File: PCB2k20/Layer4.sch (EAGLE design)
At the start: 32 parts

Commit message: Layer 4: linked with fusion so its easier to move stuff around
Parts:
- removed 1R2: 1k, JH:RESISTOR0603
- removed 1R3: 10k, JH:RESISTOR0603
- removed 1S1: 34-MOMENTARY-SWITCH, JH:34-MOMENTARY-SWITCH
- added J1, J2: CONN_03, JH:CONN_03
- added J3: (no value), SparkFun-Connectors:CONN_05LOCK
- added R1: 10k, JH:RESISTOR0603
- added U$1: 74HCT08, JH:74HCT08
- 1S2: value 34-MOMENTARY-SWITCH -> MOMENTARY_SWITCH_4X3; device JH:34-MOMENTARY-SWITCH -> JH:MOMENTARY_SWITCH_4X3
- D1, D10, D11, D12, D13, D14, D15, D16, D2, D3, D4, D5, D6, D7, D8, D9: device SparkFun-LED:WS2812B -> JH:WS2812B
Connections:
- net 15 renamed SDA
- net 16 renamed SCL
- net 17 renamed TOF3_XSHUT
- net 18 renamed TOF3_GPIO
- net 19 renamed TOF4_XSHUT
- net 20 renamed TOF4_GPIO
- net 28 renamed TOF1_XSHUT
- net 29 renamed TOF1_GPIO
- net 30 renamed TOF2_XSHUT
- net 31 renamed TOF2_GPIO
- removed net 0: 1U1.PB11/I2C2_SDA/USART3_RX
- removed net 1: 1U1.PB10/I2C2_SCL/USART3_TX
- removed net 10: 1U1.PA1/USART2_RTS/ADC12_IN1/TIM2_CH2
- removed net 11: 1U1.PA0_WKUP/USART2_CTS/ADC12_IN0/TIM2_CH1_ETR
- removed net 12: 1U1.PC15-OSC32_OUT
- removed net 13: 1U1.PC14-OSC32_IN
- removed net 14: 1U1.PC13-TAMPER-RTC
- removed net 2: 1U1.PB2/BOOT1
- removed net 23_USBDP: 1U1.PA12/USART1_RTS/CAN_TX/TIM1_ETR/USBDP
- removed net 24_USBDM: 1U1.PA11/USART1_CTS/CAN_RX/TIM1_CH4/USBDM
- removed net 25: 1U1.PA10/USART1_RX/TIM1_CH3
- removed net 26: 1U1.PA9/USART1_TX/TIM1_CH2
- removed net 27: 1U1.PA8/USART1_CK/TIM1_CH1/MCO
- removed net 3: 1U1.PB0/ADC12_IN8/TIM3_CH3
- removed net 32: 1R3.2, 1S1.2, 1U1.BOOT0, 1U1.PB8/TIM4_CH3
- removed net 4: 1U1.PA7/SPI1_MOSI/ADC12_IN7/TIM3_CH2
- removed net 5: 1U1.PA6/SPI1_MISO/ADC12_IN6/TIM3_CH1
- removed net 6: 1U1.PA5/SPI1_SCK/ADC12_IN5
- removed net 7: 1U1.PA4/SPI1_NSS/USART2_CK/ADC12_IN4
- removed net 8: 1U1.PA3/USART2_RX/ADC12_IN3/TIM2_CH4
- removed net 9: 1U1.PA2/USART2_TX/ADC12_IN2/TIM2_CH3
- removed net DISC: 1U1.PB9/TIM4_CH4
- removed net N$1: 1R2.1, 1S1.1
- removed net VBAT: 1U1.VBAT
- new net 5V: J3.5, U$1G1.I1, U$1G2.I1, U$1G3.I1, U$1G5.P$V+
- new net ESC1_IN: 1U1.PA8/USART1_CK/TIM1_CH1/MCO, U$1G2.I0
- new net ESC1_OUT: J1.3, U$1G2.O
- new net ESC2_IN: 1U1.PA1/USART2_RTS/ADC12_IN1/TIM2_CH2, U$1G3.I0
- new net ESC2_OUT: J2.3, U$1G3.O
- new net N$23: 1U1.BOOT0, R1.1
- new net USART1_RX: 1U1.PA10/USART1_RX/TIM1_CH3, J3.3
- new net USART1_TX: 1U1.PA9/USART1_TX/TIM1_CH2, J3.2
- new net WS2812B: 1U1.PA7/SPI1_MOSI/ADC12_IN7/TIM3_CH2, U$1G1.I0
- new net WS2812B_OUT: D1.DI, U$1G1.O
- net 3.3V: now also J3.4; no longer 1R2.2
- net GND: now also J1.1, J2.1, J3.1, R1.2, U$1G5.P$V-; no longer 1R3.1
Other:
- note removed: "BOOT0"
- moved on the sheet: 1D1, 1R1, SWD

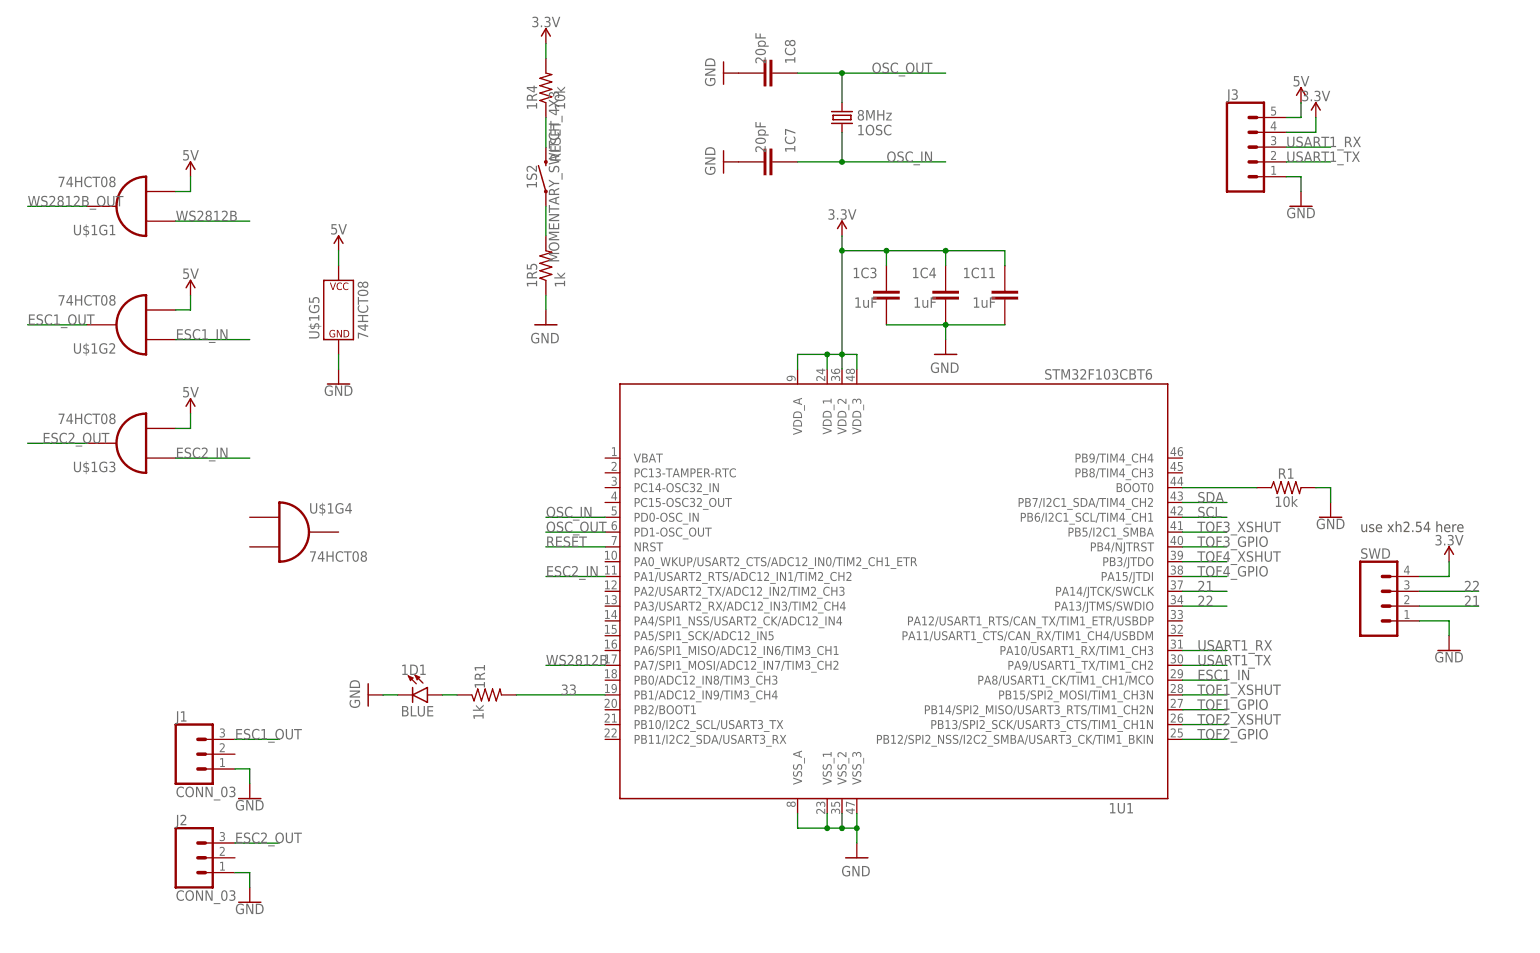
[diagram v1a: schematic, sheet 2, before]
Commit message: finish layer 4 and start on layer 3, TODO: silkscreen for layer4
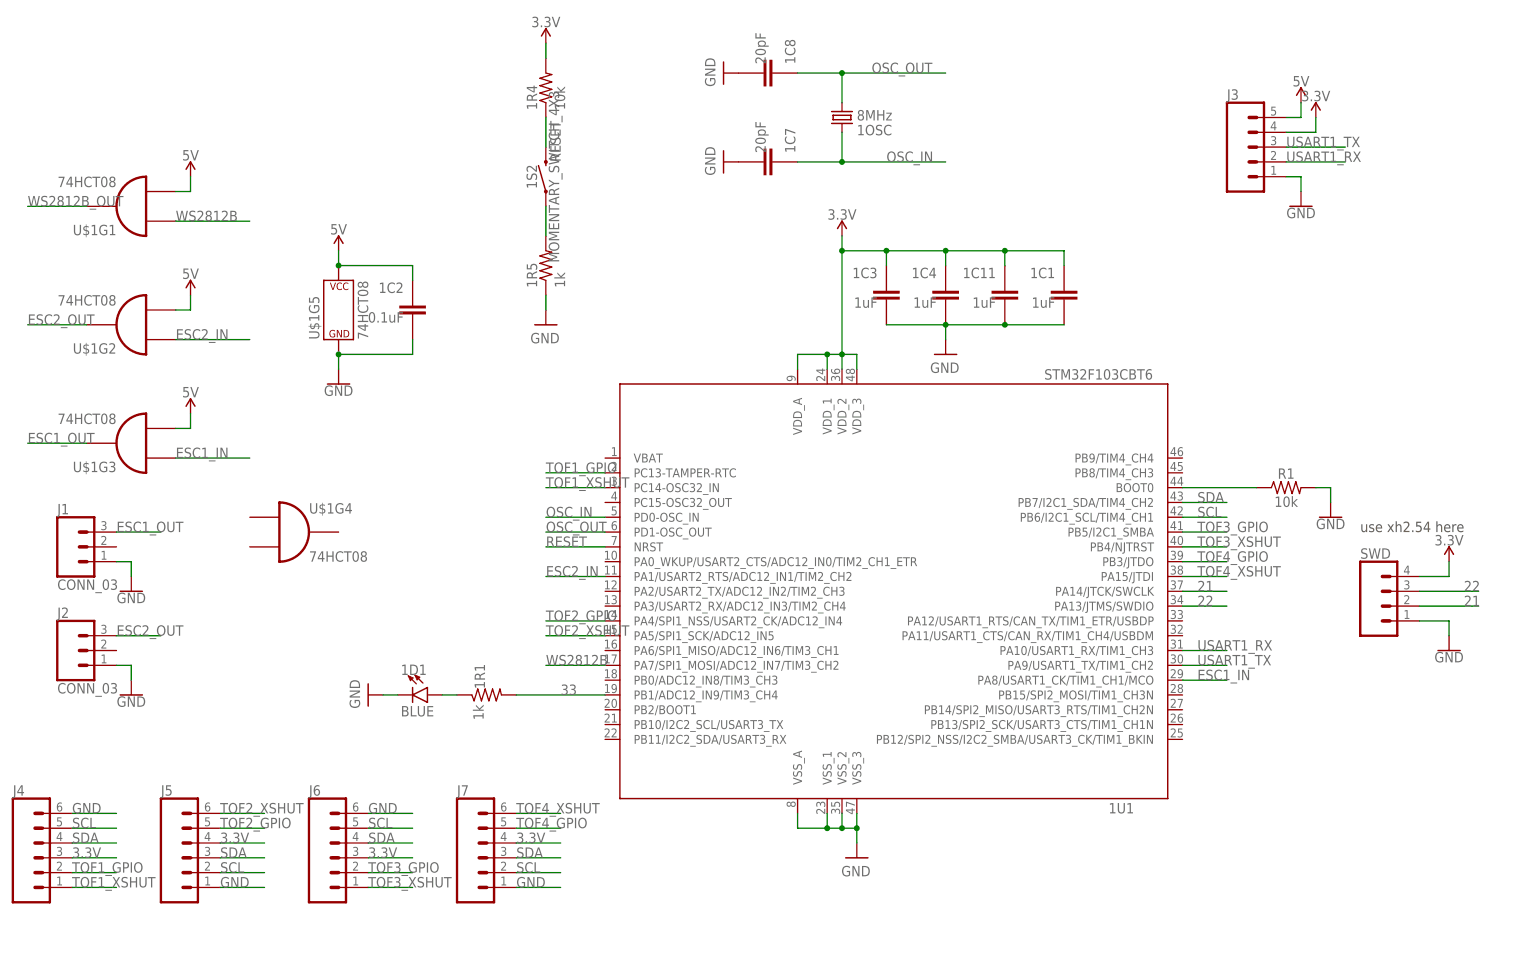
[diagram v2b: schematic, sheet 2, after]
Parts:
- added 1C1: 1uF, JH:CAPACITOR0603
- added 1C2, AC1, AC2, AC3, AC4, AC5, AC6, AC7, AC8, C1, C11, C13, C15, C3, C5, C7, C9: 0.1uF, JH:CAPACITOR0603
- added J4, J5, J6, J7: (no value), SparkFun-Connectors:CONN_06LOCK
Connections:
- net 3.3V: now also 1C1.1, J4.3, J5.4, J6.3, J7.4; no longer D1.VDD, D10.VDD, D11.VDD, D12.VDD, D13.VDD, D14.VDD, D15.VDD, D16.VDD, D2.VDD, D3.VDD, D4.VDD, D5.VDD, D6.VDD, D7.VDD, D8.VDD, D9.VDD
- net 5V: now also 1C2.1, AC1.1, AC2.1, AC3.1, AC4.1, AC5.1, AC6.1, AC7.1, AC8.1, C1.1, C11.1, C13.1, C15.1, C3.1, C5.1, C7.1, C9.1, D1.VDD, D10.VDD, D11.VDD, D12.VDD, D13.VDD, D14.VDD, D15.VDD, D16.VDD, D2.VDD, D3.VDD, D4.VDD, D5.VDD, D6.VDD, D7.VDD, D8.VDD, D9.VDD
- net ESC1_IN: now also U$1G3.I0; no longer U$1G2.I0
- net ESC1_OUT: now also U$1G3.O; no longer U$1G2.O
- net ESC2_IN: now also U$1G2.I0; no longer U$1G3.I0
- net ESC2_OUT: now also U$1G2.O; no longer U$1G3.O
- net GND: now also 1C1.2, 1C2.2, AC1.2, AC2.2, AC3.2, AC4.2, AC5.2, AC6.2, AC7.2, AC8.2, C1.2, C11.2, C13.2, C15.2, C3.2, C5.2, C7.2, C9.2, J4.6, J5.1, J6.6, J7.1
- net SCL: now also J4.5, J5.2, J6.5, J7.2
- net SDA: now also J4.4, J5.3, J6.4, J7.3
- net TOF1_GPIO: now also 1U1.PC13-TAMPER-RTC, J4.2; no longer 1U1.PB14/SPI2_MISO/USART3_RTS/TIM1_CH2N
- net TOF1_XSHUT: now also 1U1.PC14-OSC32_IN, J4.1; no longer 1U1.PB15/SPI2_MOSI/TIM1_CH3N
- net TOF2_GPIO: now also 1U1.PA4/SPI1_NSS/USART2_CK/ADC12_IN4, J5.5; no longer 1U1.PB12/SPI2_NSS/I2C2_SMBA/USART3_CK/TIM1_BKIN
- net TOF2_XSHUT: now also 1U1.PA5/SPI1_SCK/ADC12_IN5, J5.6; no longer 1U1.PB13/SPI2_SCK/USART3_CTS/TIM1_CH1N
- net TOF3_GPIO: now also 1U1.PB5/I2C1_SMBA, J6.2; no longer 1U1.PB4/NJTRST
- net TOF3_XSHUT: now also 1U1.PB4/NJTRST, J6.1; no longer 1U1.PB5/I2C1_SMBA
- net TOF4_GPIO: now also 1U1.PB3/JTDO, J7.5; no longer 1U1.PA15/JTDI
- net TOF4_XSHUT: now also 1U1.PA15/JTDI, J7.6; no longer 1U1.PB3/JTDO
- net USART1_RX: now also J3.2; no longer J3.3
- net USART1_TX: now also J3.3; no longer J3.2
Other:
- moved on the sheet: J1, J2

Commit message: done just need to silkscreen now!!!
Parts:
- added S1: (no value), SparkFun-Switches:SWITCH-SPDT-PTH-11.6X4.0MM-LOCK
- SWD: value (none) -> SM06B-SRSS-TB; device SparkFun-Connectors:CONN_04LOCK -> con-JST SH:SM06B-SRSS-TB
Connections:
- new net DEBUG_RX: 1U1.PA3/USART2_RX/ADC12_IN3/TIM2_CH4, SWD.6
- new net DEBUG_TX: 1U1.PA2/USART2_TX/ADC12_IN2/TIM2_CH3, SWD.5
- new net N$26: J3.4, S1.P
- net 3.3V: now also S1.O; no longer J3.4
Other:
- note removed: "use xh2.54 here"
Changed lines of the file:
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@@
 <part name="1OSC" library="SparkFun-Clocks" library_urn="urn:adsk.eagle:library:511" deviceset="CRYSTAL" device="SMD-5X3.2-2PAD" package3d_urn="urn:adsk.eagle:package:37520/1" value="8MHz"/>
 <part name="FRAME2" library="SparkFun-Aesthetics" library_urn="urn:adsk.eagle:library:507" deviceset="FRAME-A4L" device=""/>
-<part name="SWD" library="SparkFun-Connectors" library_urn="urn:adsk.eagle:library:513" deviceset="CONN_04" device="LOCK" package3d_urn="urn:adsk.eagle:package:38089/1"/>
+<part name="SWD" library="con-JST SH" library_urn="urn:adsk.eagle:library:17006044" deviceset="SM06B-SRSS" device="-TB" package3d_urn="urn:adsk.eagle:package:17006117/1"/>
 <part name="GND5" library="SparkFun-PowerSymbols" library_urn="urn:adsk.eagle:library:530" deviceset="GND" device=""/>
 <part name="1S2" library="JH" library_urn="urn:adsk.eagle:library:6027132" deviceset="MOMENTARY_SWITCH_4X3" device="" package3d_urn="urn:adsk.eagle:package:16673543/1"/>
@@
 <part name="SUPPLY27" library="SparkFun-PowerSymbols" library_urn="urn:adsk.eagle:library:530" deviceset="5V" device=""/>
 <part name="SUPPLY32" library="SparkFun-PowerSymbols" library_urn="urn:adsk.eagle:library:530" deviceset="5V" device=""/>
+<part name="S1" library="SparkFun-Switches" library_urn="urn:adsk.eagle:library:535" deviceset="SWITCH-SPDT" device="-PTH-11.6X4.0MM-LOCK" package3d_urn="urn:adsk.eagle:package:40181/1"/>
 </parts>
 <sheets>
@@
 <sheet>
 <plain>
-<text x="243.84" y="91.44" size="1.778" layer="97">use xh2.54 here</text>
 </plain>
 <instances>
@@
 <attribute name="SHEET" x="200.66" y="6.35" size="2.54" layer="94" font="vector"/>
 </instance>
-<instance part="SWD" gate="G$1" x="248.92" y="78.74" smashed="yes">
-<attribute name="VALUE" x="243.84" y="71.374" size="1.778" layer="96" font="vector"/>
-<attribute name="NAME" x="243.84" y="86.868" size="1.778" layer="95" font="vector"/>
+<instance part="SWD" gate="G$1" x="246.38" y="83.82" smashed="yes">
+<attribute name="VALUE" x="245.11" y="71.12" size="1.778" layer="96"/>
+<attribute name="NAME" x="245.11" y="92.202" size="1.778" layer="95"/>
 </instance>
 <instance part="GND5" gate="1" x="259.08" y="71.12" smashed="yes">
@@
 <attribute name="VALUE" x="181.356" y="129.921" size="1.778" layer="96" rot="MR0"/>
 </instance>
-<instance part="SUPPLY1" gate="G$1" x="259.08" y="86.36" smashed="yes">
-<attribute name="VALUE" x="259.08" y="89.154" size="1.778" layer="96" align="bottom-center"/>
+<instance part="SUPPLY1" gate="G$1" x="269.24" y="86.36" smashed="yes">
+<attribute name="VALUE" x="269.24" y="89.154" size="1.778" layer="96" align="bottom-center"/>
 </instance>
 <instance part="SUPPLY2" gate="G$1" x="104.14" y="175.26" smashed="yes">
@@
 <attribute name="NAME" x="220.98" y="165.608" size="1.778" layer="95" font="vector"/>
 </instance>
-<instance part="SUPPLY30" gate="G$1" x="236.22" y="162.56" smashed="yes">
-<attribute name="VALUE" x="236.22" y="165.354" size="1.778" layer="96" align="bottom-center"/>
+<instance part="SUPPLY30" gate="G$1" x="251.46" y="165.1" smashed="yes">
+<attribute name="VALUE" x="251.46" y="167.894" size="1.778" layer="96" align="bottom-center"/>
 </instance>
 <instance part="SUPPLY31" gate="G$1" x="233.68" y="165.1" smashed="yes">
@@
 <attribute name="NAME" x="79.756" y="132.461" size="1.778" layer="95" rot="MR0"/>
 <attribute name="VALUE" x="79.756" y="127.381" size="1.778" layer="96" rot="MR0"/>
+</instance>
+<instance part="S1" gate="1" x="243.84" y="160.02" smashed="yes">
+<attribute name="NAME" x="245.11" y="163.068" size="1.778" layer="95" font="vector" align="bottom-center"/>
+<attribute name="VALUE" x="244.856" y="156.718" size="1.778" layer="96" font="vector" align="top-center"/>
 </instance>
 </instances>
@@
 <pinref part="SWD" gate="G$1" pin="2"/>
 <wire x1="254" y1="78.74" x2="264.16" y2="78.74" width="0.1524" layer="91"/>
-<label x="261.62" y="78.74" size="1.778" layer="95"/>
+<label x="256.54" y="78.74" size="1.778" layer="95"/>
 </segment>
 </net>
@@
 <pinref part="SWD" gate="G$1" pin="3"/>
 <wire x1="254" y1="81.28" x2="264.16" y2="81.28" width="0.1524" layer="91"/>
-<label x="261.62" y="81.28" size="1.778" layer="95"/>
+<label x="256.54" y="81.28" size="1.778" layer="95"/>
 </segment>
 </net>
@@
 <segment>
 <pinref part="SWD" gate="G$1" pin="4"/>
-<wire x1="254" y1="83.82" x2="259.08" y2="83.82" width="0.1524" layer="91"/>
-<wire x1="259.08" y1="86.36" x2="259.08" y2="83.82" width="0.1524" layer="91"/>
+<wire x1="254" y1="83.82" x2="269.24" y2="83.82" width="0.1524" layer="91"/>
+<wire x1="269.24" y1="86.36" x2="269.24" y2="83.82" width="0.1524" layer="91"/>
 <pinref part="SUPPLY1" gate="G$1" pin="3.3V"/>
 </segment>
@@
 </segment>
 <segment>
-<pinref part="J3" gate="G$1" pin="4"/>
-<pinref part="SUPPLY30" gate="G$1" pin="3.3V"/>
-<wire x1="231.14" y1="160.02" x2="236.22" y2="160.02" width="0.1524" layer="91"/>
-<wire x1="236.22" y1="160.02" x2="236.22" y2="162.56" width="0.1524" layer="91"/>
-</segment>
-<segment>
 <pinref part="J4" gate="G$1" pin="3"/>
 <wire x1="22.86" y1="35.56" x2="30.48" y2="35.56" width="0.1524" layer="91"/>
@@
 <label x="99.06" y="38.1" size="1.778" layer="95"/>
 <pinref part="J7" gate="G$1" pin="4"/>
+</segment>
+<segment>
+<pinref part="S1" gate="1" pin="O"/>
+<pinref part="SUPPLY30" gate="G$1" pin="3.3V"/>
+<wire x1="248.92" y1="162.56" x2="251.46" y2="162.56" width="0.1524" layer="91"/>
+<wire x1="251.46" y1="162.56" x2="251.46" y2="165.1" width="0.1524" layer="91"/>
 </segment>
 </net>
@@
 </segment>
 </net>
+<net name="DEBUG_TX" class="0">
+<segment>
+<pinref part="1U1" gate="G$1" pin="PA2/USART2_TX/ADC12_IN2/TIM2_CH3"/>
+<wire x1="114.3" y1="81.28" x2="104.14" y2="81.28" width="0.1524" layer="91"/>
+<label x="104.14" y="81.28" size="1.778" layer="95"/>
+</segment>
+<segment>
+<pinref part="SWD" gate="G$1" pin="5"/>
+<wire x1="254" y1="86.36" x2="264.16" y2="86.36" width="0.1524" layer="91"/>
+<label x="256.54" y="86.36" size="1.778" layer="95"/>
+</segment>
+</net>
+<net name="DEBUG_RX" class="0">
+<segment>
+<pinref part="1U1" gate="G$1" pin="PA3/USART2_RX/ADC12_IN3/TIM2_CH4"/>
+<wire x1="114.3" y1="78.74" x2="104.14" y2="78.74" width="0.1524" layer="91"/>
+<label x="104.14" y="78.74" size="1.778" layer="95"/>
+</segment>
+<segment>
+<pinref part="SWD" gate="G$1" pin="6"/>
+<wire x1="254" y1="88.9" x2="264.16" y2="88.9" width="0.1524" layer="91"/>
+<label x="256.54" y="88.9" size="1.778" layer="95"/>
+</segment>
+</net>
+<net name="N$26" class="0">
+<segment>
+<pinref part="J3" gate="G$1" pin="4"/>
+<wire x1="231.14" y1="160.02" x2="241.3" y2="160.02" width="0.1524" layer="91"/>
+<pinref part="S1" gate="1" pin="P"/>
+</segment>
+</net>
